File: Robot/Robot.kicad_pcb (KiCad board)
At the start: 2 copper layers, 130 x 156 mm, 173 parts, among them J1 Servo1, J10 Lidar, J11 Console, J12 M1, J13 M2, J14 M3, J15 M4, J16 Battery, J17 DE9_Receptacle, J18 Balance, J2 Servo2, J3 Servo3, J4 Servo4, J5 Servo5, J6 Servo6, J7 Servo7, J8 Beacon, J9 DLED, Q1 DMP3036SSD, Q2 Si2003, SW1 User, SW2 Pwr, U1 ADC128D818, U10 SY8366HQQC, U11 SY8366HQQC, U12 SY8366HQQC, U13 INA180A2, U14 INA180A2, U15 INA180A2, U16 INA180A2, U2 MaixCAM2, U3 DRV8845RHHR, U4 ICE40UP5K-SG48ITR, U5 74HCT245, U6 MCP4728, U7 NC7SZ175, U8 TLV70212DBVR, U9 TMI6050-33

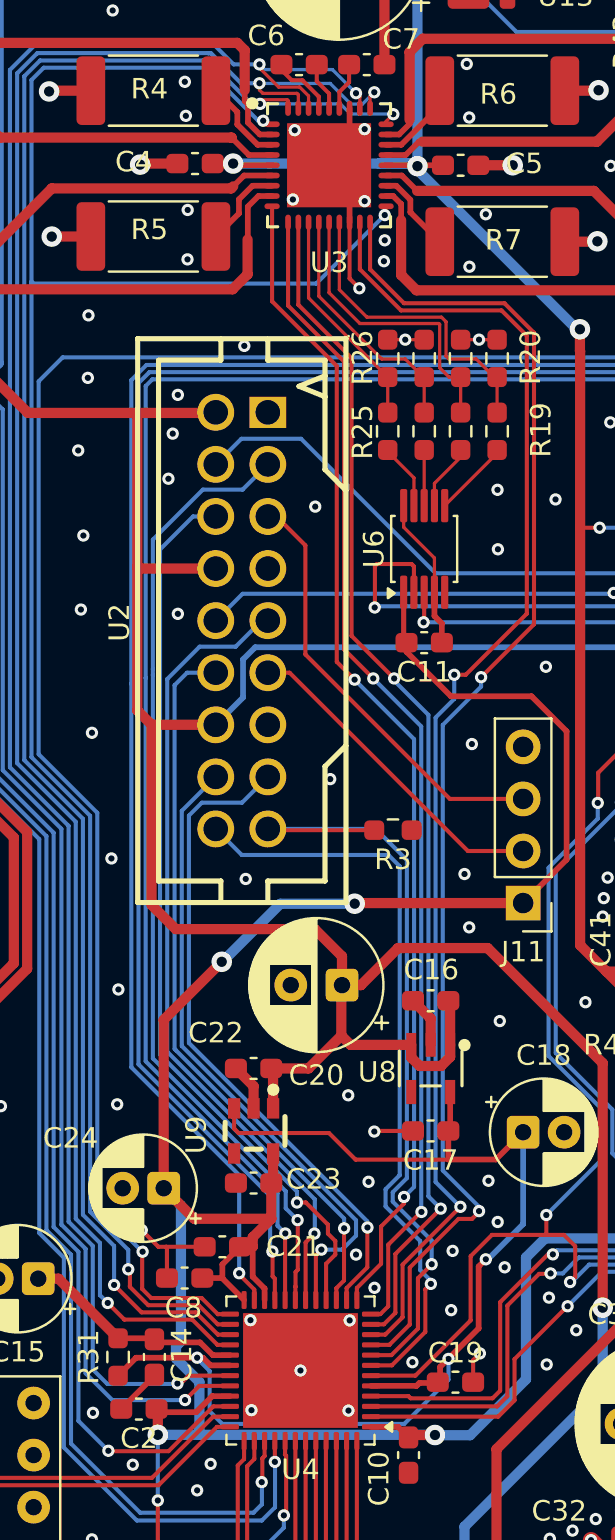
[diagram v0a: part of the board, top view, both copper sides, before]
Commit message: Added 3D models of stands (both corner and middle). Also created patterns for all stands for side panels
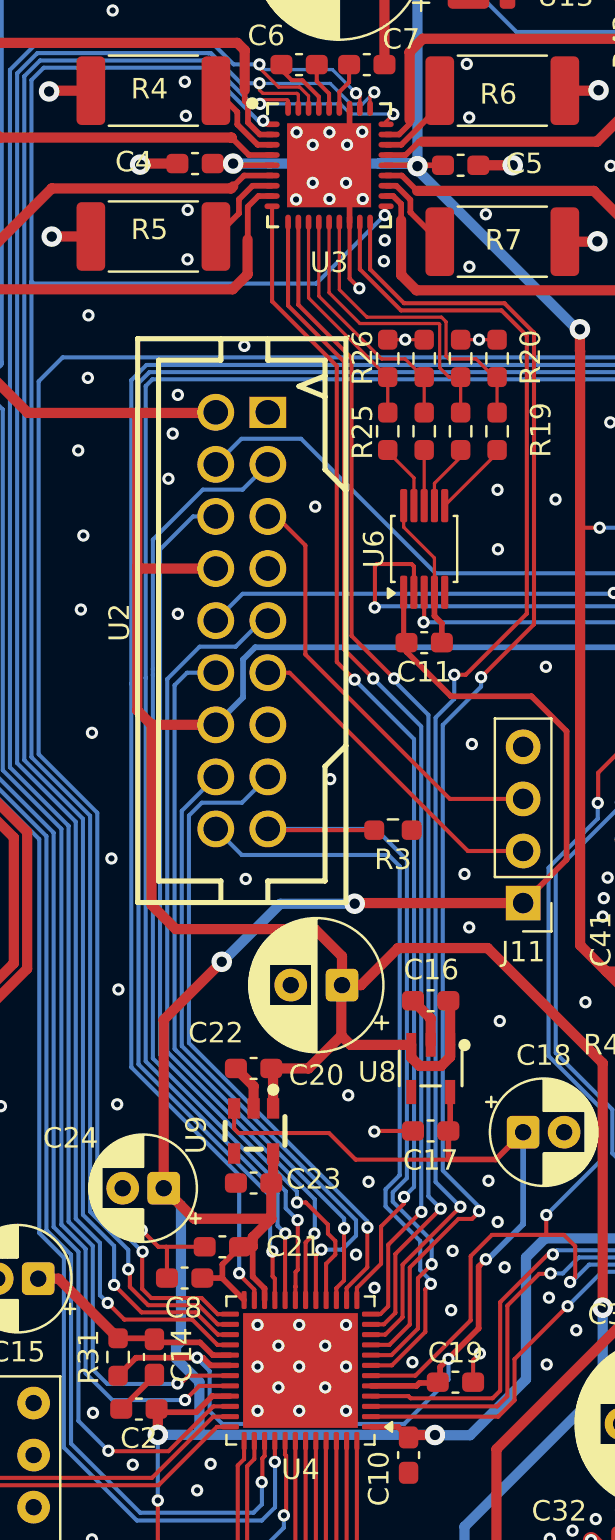
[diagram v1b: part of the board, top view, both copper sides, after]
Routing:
- net GND: vias 374 -> 388
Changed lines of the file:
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@@
 		)
 		(property "Value" "0.018"
-			(at 0 2.65 -90)
+			(at 0 2.65 270)
 			(layer "F.Fab")
 			(effects
@@
 		)
 		(fp_text user "${REFERENCE}"
-			(at 0 0 -90)
+			(at 0 0 270)
 			(layer "F.Fab")
 			(effects
@@
 		(tags "resistor handsolder")
 		(property "Reference" "R43"
-			(at -3.302 0 -90)
+			(at -3.302 0 270)
 			(layer "F.SilkS")
 			(effects
@@
 		)
 		(property "Value" "10K"
-			(at 0 1.43 -90)
+			(at 0 1.43 270)
 			(layer "F.Fab")
 			(effects
@@
 		)
 		(fp_text user "${REFERENCE}"
-			(at 0 0 -90)
+			(at 0 0 270)
 			(layer "F.Fab")
 			(effects
@@
 		(tags "resistor handsolder")
 		(property "Reference" "R42"
-			(at -0.0425 1.684 -90)
+			(at -0.0425 1.684 270)
 			(layer "F.SilkS")
 			(effects
@@
 		)
 		(property "Value" "10K"
-			(at 0 1.43 -90)
+			(at 0 1.43 270)
 			(layer "F.Fab")
 			(effects
@@
 		)
 		(fp_text user "${REFERENCE}"
-			(at 0 0 -90)
+			(at 0 0 270)
 			(layer "F.Fab")
 			(effects
@@
 		)
 		(property "Value" "INA180A2"
-			(at 0 2.9 -90)
+			(at 0 2.9 270)
 			(layer "F.Fab")
 			(effects
@@
 		(tags "capacitor handsolder")
 		(property "Reference" "C43"
-			(at 3.302 -0.254 -90)
+			(at 3.302 -0.254 270)
 			(layer "F.SilkS")
 			(effects
@@
 		)
 		(property "Value" "2.2"
-			(at 0 1.43 -90)
+			(at 0 1.43 270)
 			(layer "F.Fab")
 			(effects
@@
 		)
 		(fp_text user "${REFERENCE}"
-			(at 0 0 -90)
+			(at 0 0 270)
 			(layer "F.Fab")
 			(effects
@@
 		(tags "capacitor handsolder")
 		(property "Reference" "C44"
-			(at 0 1.43 -90)
+			(at 0 1.43 270)
 			(layer "B.SilkS")
 			(effects
@@
 		)
 		(property "Value" "1.0"
-			(at 0 -1.43 -90)
+			(at 0 -1.43 270)
 			(layer "B.Fab")
 			(effects
@@
 		)
 		(fp_text user "${REFERENCE}"
-			(at 0 0 -90)
+			(at 0 0 270)
 			(layer "B.Fab")
 			(effects
@@
 	)
 	(via
+		(at 115.068 133.35)
+		(size 0.6)
+		(drill 0.3)
+		(layers "F.Cu" "B.Cu")
+		(net 1)
+	)
+	(via
 		(at 130.766651 142.38)
 		(size 0.6)
@@
 	)
 	(via
-		(at 112.69 133.12)
+		(at 113.036 133.35)
 		(size 0.6)
 		(drill 0.3)
@@
 	)
 	(via
-		(at 117.53 133.13)
+		(at 117.354 133.35)
 		(size 0.6)
 		(drill 0.3)
@@
 	)
 	(via
+		(at 115.7284 77.6478)
+		(size 0.6)
+		(drill 0.3)
+		(layers "F.Cu" "B.Cu")
+		(net 1)
+	)
+	(via
 		(at 38.05 162.03)
 		(size 0.6)
@@
 	)
 	(via
+		(at 117.4048 75.7936)
+		(size 0.6)
+		(drill 0.3)
+		(layers "F.Cu" "B.Cu")
+		(net 1)
+	)
+	(via
 		(at 105.01 137.64)
 		(size 0.6)
@@
 	)
 	(via
+		(at 116.338 134.366)
+		(size 0.6)
+		(drill 0.3)
+		(layers "F.Cu" "B.Cu")
+		(net 1)
+	)
+	(via
 		(at 36.6 73.17)
 		(size 0.6)
@@
 	)
 	(via
+		(at 115.068 137.541)
+		(size 0.6)
+		(drill 0.3)
+		(layers "F.Cu" "B.Cu")
+		(net 1)
+	)
+	(via
 		(at 132.322 110.794)
 		(size 0.6)
@@
 	)
 	(via
-		(at 118.26 75.03)
+		(at 118.1414 75.1586)
 		(size 0.6)
 		(drill 0.3)
@@
 	)
 	(via
+		(at 113.036 135.382)
+		(size 0.6)
+		(drill 0.3)
+		(layers "F.Cu" "B.Cu")
+		(net 1)
+	)
+	(via
 		(at 109.15 87.99)
 		(size 0.6)
@@
 	)
 	(via
+		(at 116.5412 78.4352)
+		(size 0.6)
+		(drill 0.3)
+		(layers "F.Cu" "B.Cu")
+		(net 1)
+	)
+	(via
 		(at 36.52 68.89)
 		(size 0.6)
@@
 	)
 	(via
-		(at 112.74 137.51)
+		(at 116.338 136.398)
+		(size 0.6)
+		(drill 0.3)
+		(layers "F.Cu" "B.Cu")
+		(net 1)
+	)
+	(via
+		(at 113.036 137.541)
 		(size 0.6)
 		(drill 0.3)
@@
 	)
 	(via
-		(at 114.76 78.46)
+		(at 114.9156 78.46)
 		(size 0.6)
 		(drill 0.3)
@@
 	)
 	(via
-		(at 117.47 137.53)
+		(at 117.354 137.541)
 		(size 0.6)
 		(drill 0.3)
@@
 	)
 	(via
+		(at 114.052 134.366)
+		(size 0.6)
+		(drill 0.3)
+		(layers "F.Cu" "B.Cu")
+		(net 1)
+	)
+	(via
 		(at 147.25 60.44)
 		(size 1)
@@
 	)
 	(via
-		(at 118.26 78.54)
+		(at 118.1668 78.4352)
 		(size 0.6)
 		(drill 0.3)
@@
 	)
 	(via
+		(at 117.354 135.382)
+		(size 0.6)
+		(drill 0.3)
+		(layers "F.Cu" "B.Cu")
+		(net 1)
+	)
+	(via
 		(at 141.272 123.704)
 		(size 0.6)
@@
 	)
 	(via
-		(at 115.13 135.574)
+		(at 116.5412 75.184)
+		(size 0.6)
+		(drill 0.3)
+		(layers "F.Cu" "B.Cu")
+		(net 1)
+	)
+	(via
+		(at 115.068 135.382)
 		(size 0.6)
 		(drill 0.3)
@@
 	)
 	(via
+		(at 115.7284 75.7936)
+		(size 0.6)
+		(drill 0.3)
+		(layers "F.Cu" "B.Cu")
+		(net 1)
+	)
+	(via
 		(at 156.15 51.12)
 		(size 0.6)
@@
 	)
 	(via
-		(at 114.85 75.08)
+		(at 114.052 136.398)
+		(size 0.6)
+		(drill 0.3)
+		(layers "F.Cu" "B.Cu")
+		(net 1)
+	)
+	(via
+		(at 114.941 75.184)
 		(size 0.6)
 		(drill 0.3)
@@
 		(net 1)
 	)
+	(via
+		(at 117.354 77.6478)
+		(size 0.6)
+		(drill 0.3)
+		(layers "F.Cu" "B.Cu")
+		(net 1)
+	)

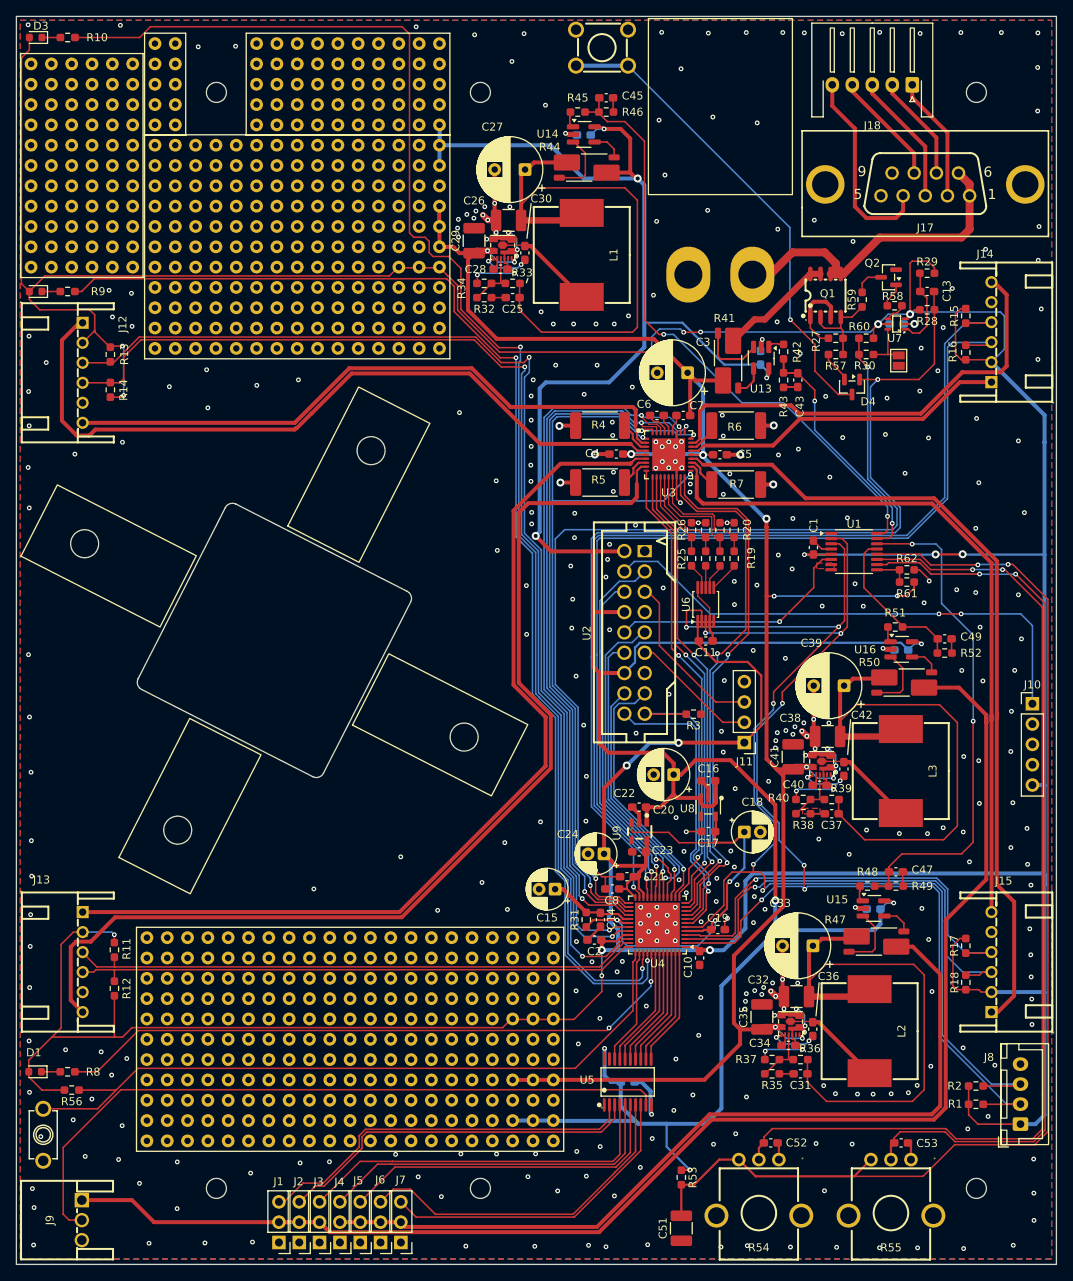
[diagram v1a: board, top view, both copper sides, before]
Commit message: Updated TPL and symbols
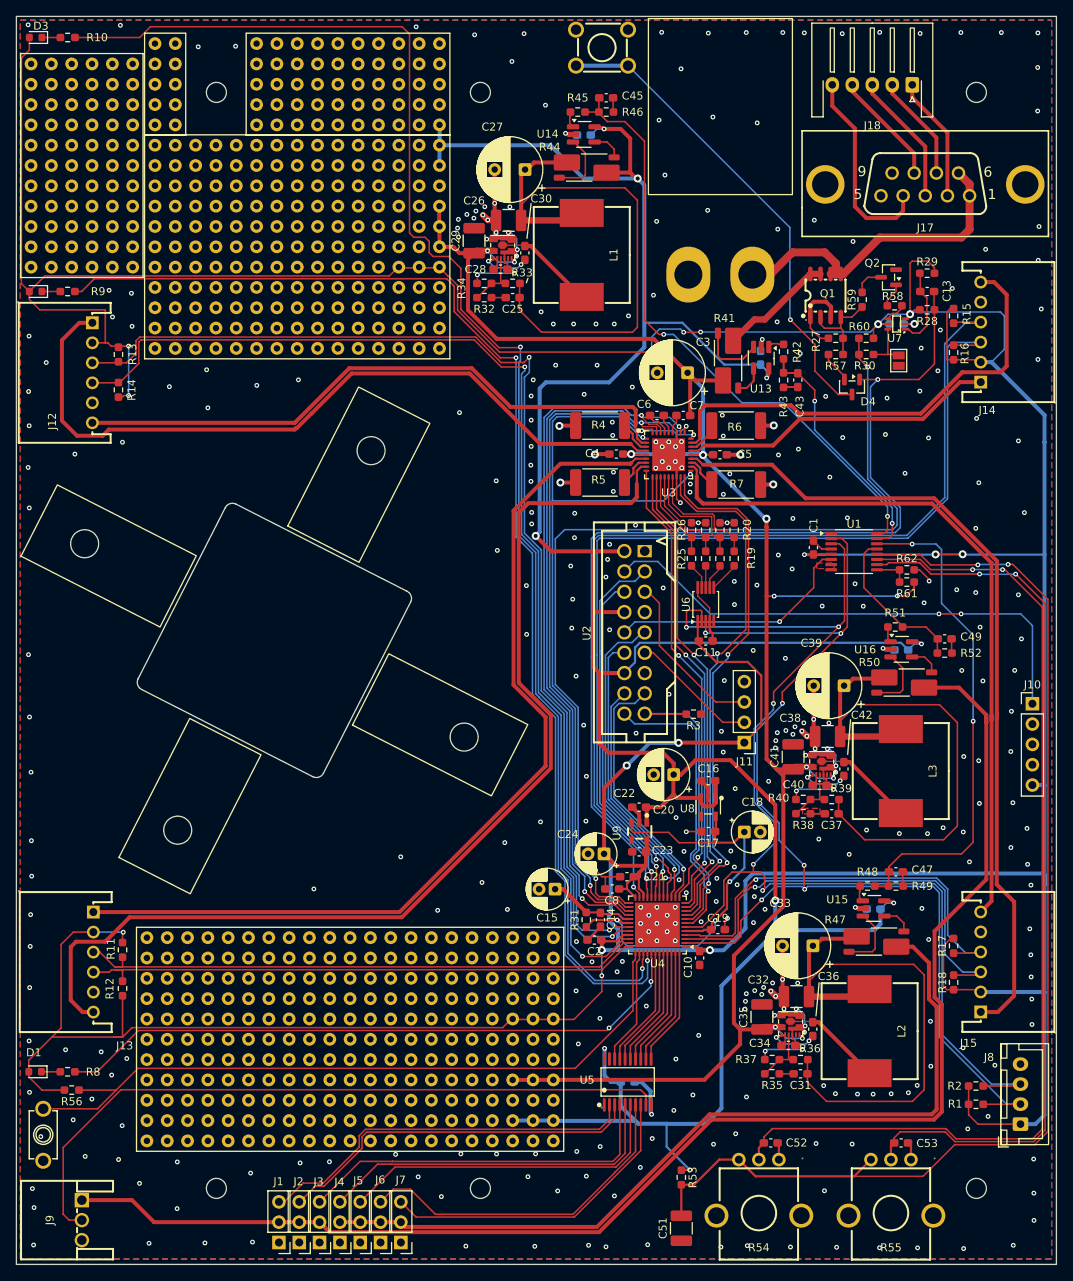
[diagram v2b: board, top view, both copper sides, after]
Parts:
- J12, J13, J14, J15: footprint locals:CONN-TH_S6B-XH-A-1-LF-SN -> locals:CONN-TH_S6B-XH-A-LF-SN
- moved R17 1.52 mm to (152.2, 138.2)
- moved R18 1.52 mm to (152.2, 142.7)
- moved R15 1.52 mm to (152.2, 59.4)
- moved R16 1.52 mm to (152.2, 64.0)
- moved J15 1.35 mm to (155.5, 140.2), turned to -90 degrees
- moved J14 1.34 mm to (155.5, 61.5), turned to -90 degrees
- moved J13 1.34 mm to (44.6, 140.2), turned to 90 degrees
- moved J12 1.22 mm to (44.5, 66.6), turned to 90 degrees
- moved R13 1.02 mm to (47.8, 64.3)
- moved R14 1.02 mm to (47.8, 68.7)
- moved R11 1.02 mm to (48.3, 138.7)
- moved R12 1.02 mm to (48.3, 143.5)
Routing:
- net +3V3: track 661.6 -> 665.4 mm
- net /FPGA/FPGACore/P21: track 122.9 -> 121.5 mm
- net /FPGA/FPGACore/P20: track 121.5 -> 120.0 mm
- net Net-(J15B-M-): track 102.5 -> 103.8 mm
- net Net-(J13B-M+): track 131.9 -> 133.2 mm
- net Net-(J14B-M-): track 41.1 -> 39.8 mm
- net Net-(J13B-M-): track 118.3 -> 117.0 mm
- net Net-(J14B-M+): track 57.8 -> 59.2 mm
- net Net-(J12B-M+): track 79.1 -> 77.9 mm
- net Net-(J12B-M-): track 94.6 -> 95.8 mm
- net /FPGA/FPGACore/P4: track 54.5 -> 53.3 mm
- net /FPGA/FPGACore/P34: track 144.3 -> 143.2 mm
- net /FPGA/FPGACore/P3: track 56.7 -> 55.8 mm
- net /Power/Pwr2: track 176.5 -> 177.2 mm
- net Net-(J15B-M+): track 88.2 -> 88.8 mm
